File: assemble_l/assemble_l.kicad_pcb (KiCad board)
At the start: 2 copper layers, 134.9 x 119.3 mm, 57 parts, among them J1 Conn_01x02_Pin, SW1 SW_Push, SW10 SW_Push, SW11 SW_Push, SW12 SW_Push, SW13 SW_Push, SW14 SW_Push, SW15 SW_Push, SW16 SW_Push, SW17 SW_Push, SW18 SW_Push, SW19 SW_Push, SW2 SW_Push, SW20 SW_Push, SW21 SW_Push, SW22 SW_Push, SW23 SW_Push, SW24 SW_Push, SW25 SW_Push, SW26 SW_Push, SW27 SW_Push, SW28 SW_Push, SW3 SW_Push, SW4 SW_Push, SW5 SW_Push, SW6 SW_Push, SW7 SW_Push, SW8 SW_Push, SW9 SW_Push, U1 Micon_BLEMicroPro

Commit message: feat: add switch plate
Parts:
- moved SW28 67.4 mm to (174.0, 100.5), turned to 90 degrees
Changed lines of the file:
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@@
 	(footprint "kbd_Parts:ResetSW"
 		(layer "F.Cu")
-		(at 141.5 41.5)
+		(at 174 100.5 90)
 		(property "Reference" "SW28"
-			(at 0 2.55 0)
+			(at 0 2.55 90)
 			(layer "F.SilkS")
 			(hide yes)
@@
 		)
 		(property "Value" "SW_Push"
-			(at 0 -2.55 0)
+			(at 0 -2.55 90)
 			(layer "F.Fab")
 			(effects
@@
 		)
 		(property "Datasheet" ""
-			(at 0 0 0)
+			(at 0 0 90)
 			(layer "F.Fab")
 			(hide yes)
@@
 		)
 		(property "Description" "Push button switch, generic, two pins"
-			(at 0 0 0)
+			(at 0 0 90)
 			(layer "F.Fab")
 			(hide yes)
@@
 		(attr through_hole)
 		(fp_line
-			(start -3 -1.75)
-			(end 3 -1.75)
+			(start 3 -1.75)
+			(end 3 -1.5)
 			(stroke
 				(width 0.15)
@@
 		)
 		(fp_line
-			(start -3 -1.5)
-			(end -3 -1.75)
+			(start -3 -1.75)
+			(end 3 -1.75)
 			(stroke
 				(width 0.15)
@@
 		)
 		(fp_line
-			(start -3 1.75)
-			(end -3 1.5)
+			(start -3 -1.5)
+			(end -3 -1.75)
 			(stroke
 				(width 0.15)
@@
 		)
 		(fp_line
-			(start 3 -1.75)
-			(end 3 -1.5)
+			(start 3 1.5)
+			(end 3 1.75)
 			(stroke
 				(width 0.15)
@@
 		)
 		(fp_line
-			(start 3 1.5)
-			(end 3 1.75)
+			(start 3 1.75)
+			(end -3 1.75)
 			(stroke
 				(width 0.15)
@@
 		)
 		(fp_line
-			(start 3 1.75)
-			(end -3 1.75)
+			(start -3 1.75)
+			(end -3 1.5)
 			(stroke
 				(width 0.15)
@@
 		)
 		(fp_text user "RESET"
-			(at 0.127 0 0)
+			(at 0.127 0 90)
 			(layer "B.SilkS")
 			(effects
@@
 		)
 		(pad "1" thru_hole circle
-			(at 3.25 0)
+			(at 3.25 0 90)
 			(size 2 2)
 			(drill 1.3)
@@
 		)
 		(pad "2" thru_hole circle
-			(at -3.25 0)
+			(at -3.25 0 90)
 			(size 2 2)
 			(drill 1.3)
@@
 		)
 		(fp_line
-			(start -6.549999 5.97)
+			(start -6.549998 5.97)
 			(end -6.55 1.65)
 			(stroke
@@
 		(fp_line
 			(start -2.5 6.849999)
-			(end -2.499999 1.949999)
+			(end -2.499998 1.949999)
 			(stroke
 				(width 0.15)
@@
 		)
 		(fp_line
-			(start -2.45 2.4)
+			(start -2.449999 2.4)
 			(end -2.45 2.076887)
 			(stroke
@@
 		)
 		(fp_line
-			(start -0.85 8.2)
+			(start -0.85 8.200001)
 			(end -0.85 3.6)
 			(stroke
@@
 		)
 		(fp_line
-			(start 0.2 8.200001)
+			(start 0.199999 8.200001)
 			(end 0.2 3.6)
 			(stroke
@@
 		(fp_line
 			(start 0.35 8.2)
-			(end 0.350001 3.600001)
+			(end 0.350001 3.600002)
 			(stroke
 				(width 0.15)
@@
 		)
 		(fp_line
-			(start 1.550001 7.95)
+			(start 1.550001 7.950001)
 			(end 1.55 3.83)
 			(stroke
@@
 			(start -1.275 3.575)
 			(mid -2.10585 3.23085)
-			(end -2.45 2.4)
+			(end -2.449999 2.4)
 			(stroke
 				(width 0.15)
@@
 		(fp_line
 			(start 2.7 -0.75)
-			(end -2.699999 -0.75)
+			(end -2.699998 -0.75)
 			(stroke
 				(width 0.15)
@@
 		)
 		(fp_line
-			(start -2.699999 -0.75)
+			(start -2.699998 -0.75)
 			(end -2.7 0.75)
 			(stroke
@@
 		)
 		(fp_line
-			(start 2.699999 0.75)
+			(start 2.699998 0.75)
 			(end 2.7 -0.75)
 			(stroke
@@
 		(fp_line
 			(start -2.7 0.75)
-			(end 2.699999 0.75)
+			(end 2.699998 0.75)
 			(stroke
 				(width 0.15)
@@
 		(fp_line
 			(start -5.65 6)
-			(end -5.65 1.400001)
+			(end -5.65 1.400002)
 			(stroke
 				(width 0.15)
@@
 		(fp_line
 			(start -4.6 6)
-			(end -4.599999 1.4)
+			(end -4.599998 1.4)
 			(stroke
 				(width 0.15)
@@
 		(fp_line
 			(start 1.3 3.575001)
-			(end -1.275 3.575001)
+			(end -1.275 3.575002)
 			(stroke
 				(width 0.15)
@@
 		)
 		(fp_arc
-			(start -1.275 3.575001)
+			(start -1.275 3.575002)
 			(mid -2.10585 3.23085)
 			(end -2.45 2.4)

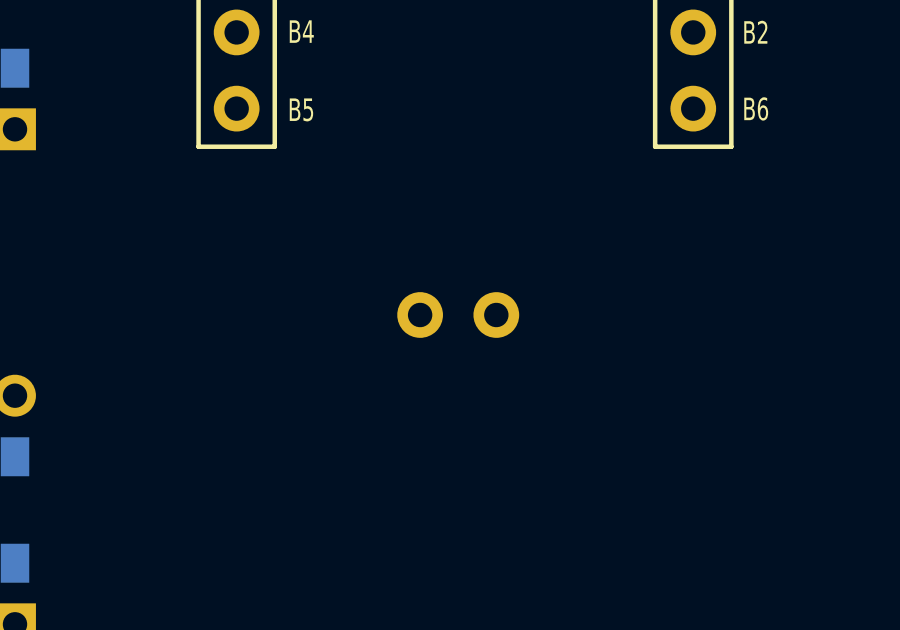
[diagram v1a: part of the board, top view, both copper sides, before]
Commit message: fix: DRC error
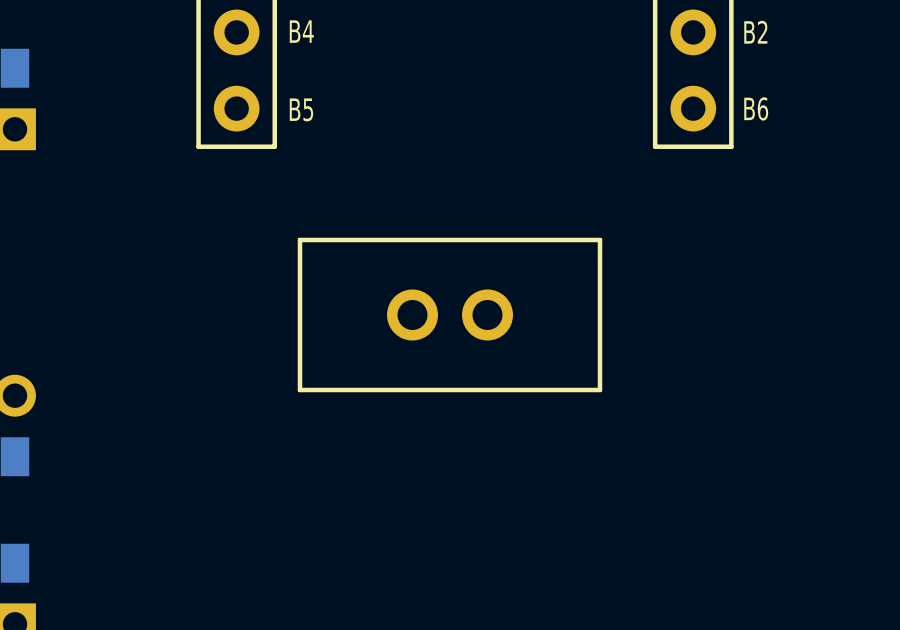
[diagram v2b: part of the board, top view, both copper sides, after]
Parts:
- J1: footprint kbd_Parts:Battery_BMP_2pin -> kbd_Parts:Battery_2pin
- turned J1 to 180 degrees

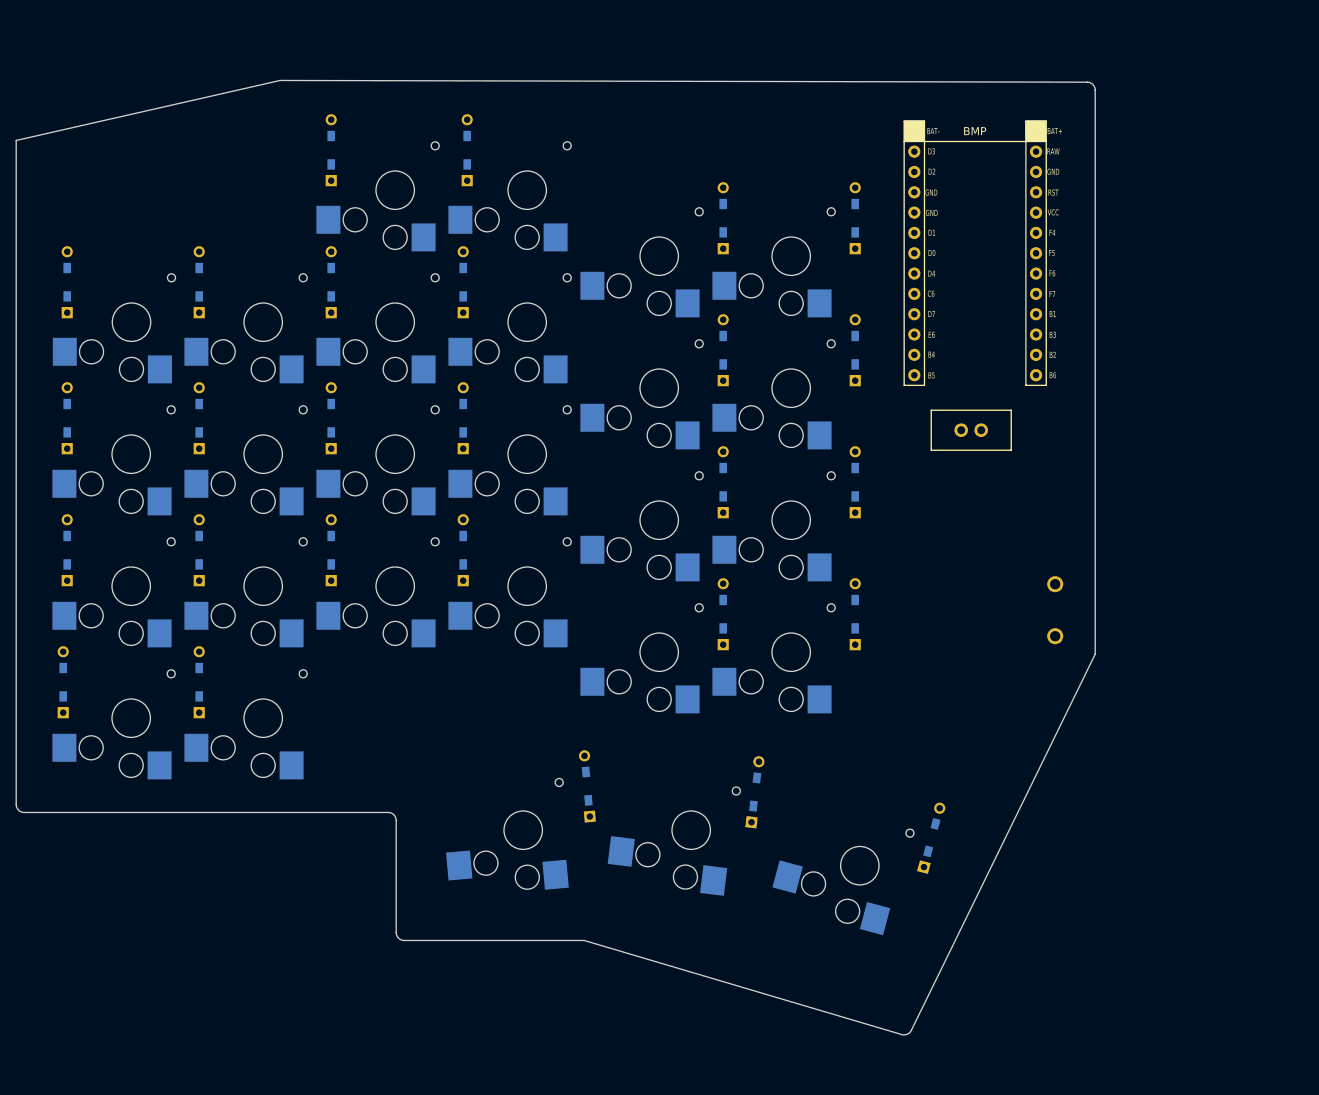
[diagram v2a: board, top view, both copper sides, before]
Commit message: feat: add hole to switch plate
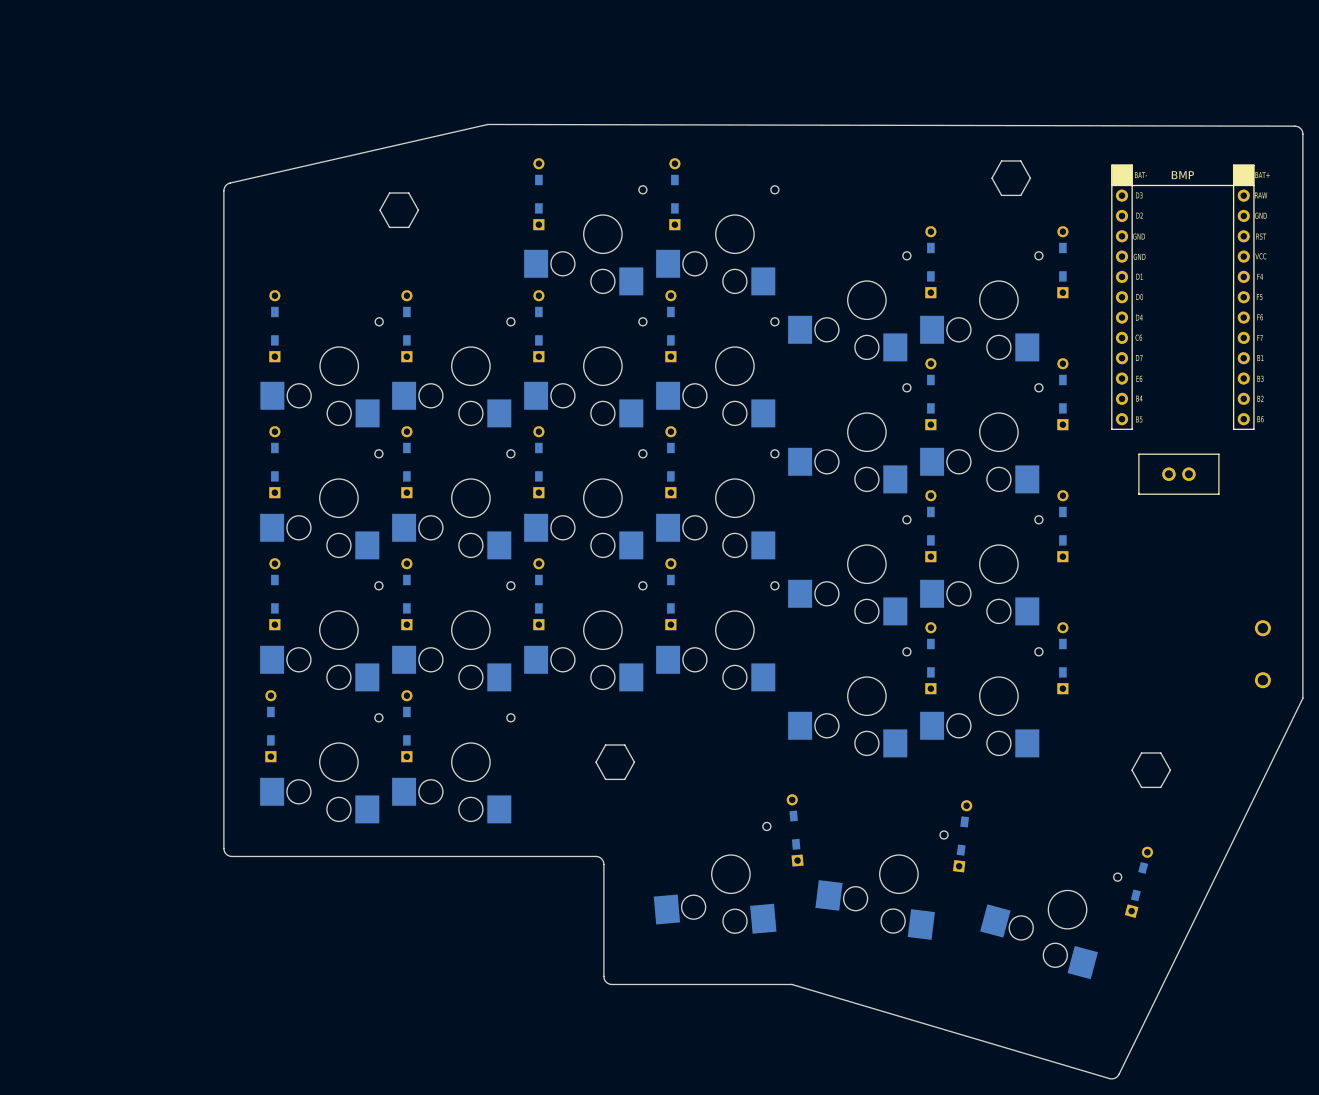
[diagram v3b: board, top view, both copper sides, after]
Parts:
- added Ref**: Val**, kbd_Hole:m2_Spacer_Hole_hex, F.Cu at (186.0, 120.5)
- added Ref**: Val**, kbd_Hole:m2_Spacer_Hole_hex, F.Cu at (92.0, 50.5)
- added Ref**: Val**, kbd_Hole:m2_Spacer_Hole_hex, F.Cu at (119.0, 119.5)
- added Ref**: Val**, kbd_Hole:m2_Spacer_Hole_hex, F.Cu at (168.5, 46.5)
- moved D1 26.5 mm to (76.5, 65.0)
- moved D10 26.5 mm to (126.0, 65.0)
- moved D11 26.5 mm to (158.5, 73.5)
- moved D12 26.5 mm to (175.0, 73.5)
- moved D13 26.5 mm to (76.5, 98.5)
- moved D14 26.5 mm to (93.0, 98.5)
- moved D15 26.5 mm to (109.5, 82.0)
- moved D16 26.5 mm to (126.0, 82.0)
- moved D17 26.5 mm to (158.5, 90.0)
- moved D18 26.5 mm to (175.0, 90.0)
- moved D19 26.5 mm to (76.0, 115.0)
- moved D2 26.5 mm to (93.0, 65.0)
- moved D20 26.5 mm to (93.0, 115.0)
- moved D21 26.5 mm to (109.5, 98.5)
- moved D22 26.5 mm to (126.0, 98.5)
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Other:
- outline, holes or cut-outs redrawn

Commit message: feat: reallocate keys on left
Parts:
- removed D22, D23, D24, D25, D26, D27: D, kbd_Parts:Diode_TH_SMD
- removed Ref** (x4): Val**, kbd_Hole:m2_Spacer_Hole_hex
- removed SW23, SW24, SW25, SW26, SW27: SW_Push, kbd_SW:Choc_v2_Hotswap_1u_16.5
- removed SW28: SW_Push, kbd_Parts:ResetSW
- SW22: footprint kbd_SW:Choc_v2_Hotswap_1u_16.5 -> kbd_Parts:ResetSW
- moved D6 99.7 mm to (77.0, 75.5)
- moved D19 88.6 mm to (143.0, 57.0)
- moved SW19 88.2 mm to (150.5, 61.0)
- moved SW6 84.6 mm to (84.5, 80.5)
- moved D5 81.5 mm to (77.0, 59.2)
- moved D14 68.7 mm to (126.5, 38.5)
- moved SW14 68.1 mm to (134.0, 43.5)
- moved SW5 66.0 mm to (84.5, 64.0)
- moved D20 65.7 mm to (143.0, 72.5)
- moved D12 65.2 mm to (110.0, 67.5)
- moved SW20 64.9 mm to (150.5, 77.5)
- moved D18 59.5 mm to (143.0, 39.8)
- moved SW3 54.6 mm to (84.5, 97.0)
- moved D3 54.3 mm to (77.0, 92.0)
- moved D11 53.4 mm to (110.0, 51.0)
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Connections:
- D10 pad 1: Row1 -> Row0
- D12 pad 1: Row1 -> Row2
- D13 pad 1: Row2 -> Row3
- D14 pad 1: Row2 -> Row0
- D15 pad 1: Row2 -> Row1
- D17 pad 1: Row2 -> Row3
- D18 pad 1: Row2 -> Row0
- D19 pad 1: Row3 -> Row1
- D2 pad 1: Row0 -> Row1
- D20 pad 1: Row3 -> Row2
- D3 pad 1: Row0 -> Row2
- D5 pad 1: Row0 -> Row1
- D6 pad 1: Row0 -> Row2
- D7 pad 1: Row1 -> Row0
- D9 pad 1: Row1 -> Row2
- SW11 pad 1: Col4 -> Col3
- SW12 pad 1: Col5 -> Col3
- SW13 pad 1: Col0 -> Col3
- SW14 pad 1: Col1 -> Col4
- SW15 pad 1: Col2 -> Col4
- SW16 pad 1: Col3 -> Col4
- SW19 pad 1: Col0 -> Col5
- SW2 pad 1: Col1 -> Col0
- SW20 pad 1: Col1 -> Col5
- SW21 pad 1: Col2 -> Col5
- SW22 pad 1: Col3 -> Reset
- SW22 pad 2: Net-(D22-A) -> GND
- SW3 pad 1: Col2 -> Col0
- SW4 pad 1: Col3 -> Col1
- SW5 pad 1: Col4 -> Col1
- SW6 pad 1: Col5 -> Col1
- SW7 pad 1: Col0 -> Col2
- SW8 pad 1: Col1 -> Col2
- U1 pad 11: Row4 -> unconnected-(U1-B4/PIN11-Pad11)
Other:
- board outline removed

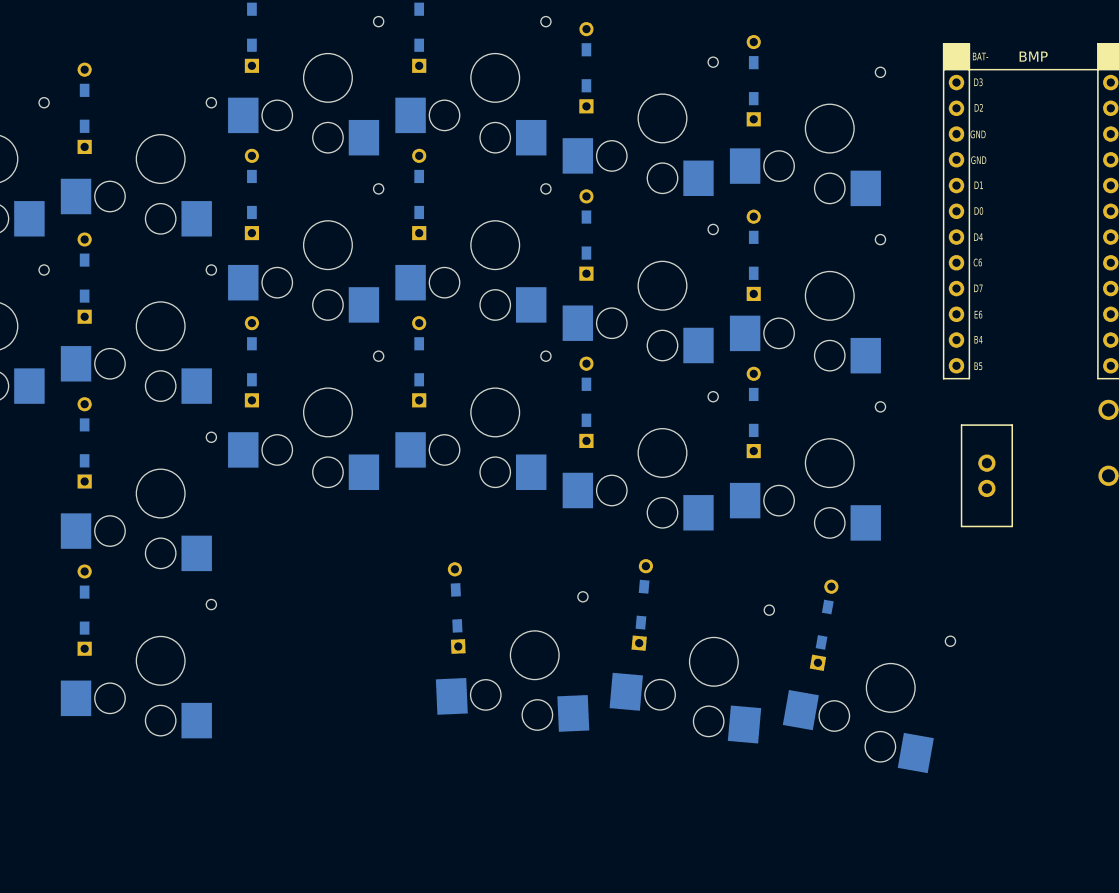
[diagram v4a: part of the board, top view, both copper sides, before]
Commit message: feat: change key placement
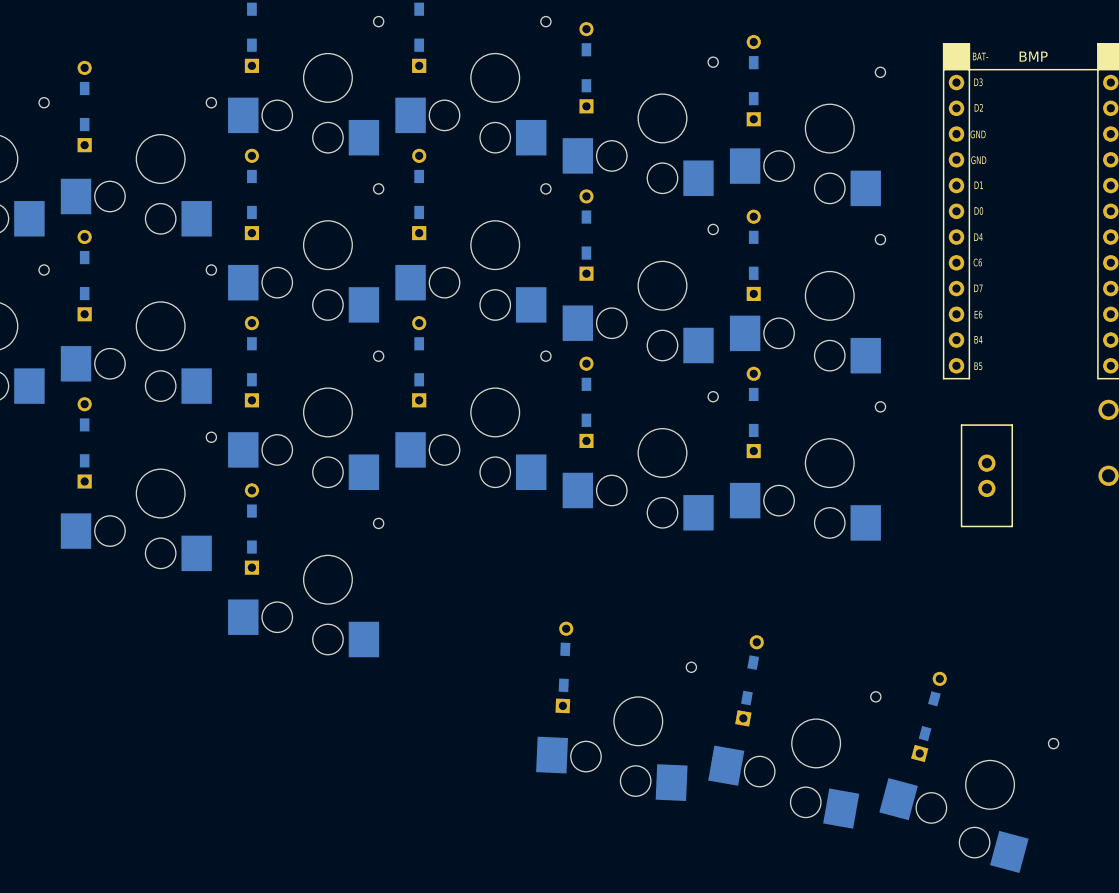
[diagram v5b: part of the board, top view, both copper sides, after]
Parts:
- moved D3 49.7 mm to (77.0, 42.3)
- moved SW3 49.5 mm to (84.5, 47.5)
- moved D6 44.2 mm to (93.5, 34.5)
- moved SW6 44.2 mm to (101.0, 39.5)
- moved D4 16.5 mm to (77.0, 59.0)
- moved D7 16.5 mm to (93.5, 51.0)
- moved D8 16.5 mm to (93.5, 67.5)
- moved D9 16.5 mm to (93.5, 84.0)
- moved SW4 16.5 mm to (84.5, 64.0)
- moved SW5 16.5 mm to (84.5, 80.5)
- moved SW7 16.5 mm to (101.0, 56.0)
- moved SW8 16.5 mm to (101.0, 72.5)
- moved SW9 16.5 mm to (101.0, 89.0)
- moved D5 16.2 mm to (77.0, 75.5)
- moved D21 13.7 mm to (160.4, 102.5), turned to 75 degrees
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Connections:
- D3 pad 1: Row2 -> Row0
- D4 pad 1: Row0 -> Row1
- D5 pad 1: Row1 -> Row2
- D6 pad 1: Row2 -> Row0
- D7 pad 1: Row0 -> Row1
- D8 pad 1: Row1 -> Row2
- D9 pad 1: Row2 -> Row3
- SW3 pad 1: Col0 -> Col1
- SW6 pad 1: Col1 -> Col2
